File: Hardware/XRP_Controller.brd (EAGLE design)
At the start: 63.5 x 54 mm, 222 parts, among them J1 POWER_JACKPOWER_JACK_SLOT, J12 Vertical Qwiic Connector, J13 Vertical Qwiic Connector, J14 Vertical Qwiic Connector, J3 JST_6_PIN_VERTICAL, J4 JST_6_PIN_VERTICAL, J5 JST_6_PIN_VERTICAL, J6 JST_6_PIN_VERTICAL, J9 Vertical Qwiic Connector, Q3 20V/4.2A/52mΩ/1.4W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

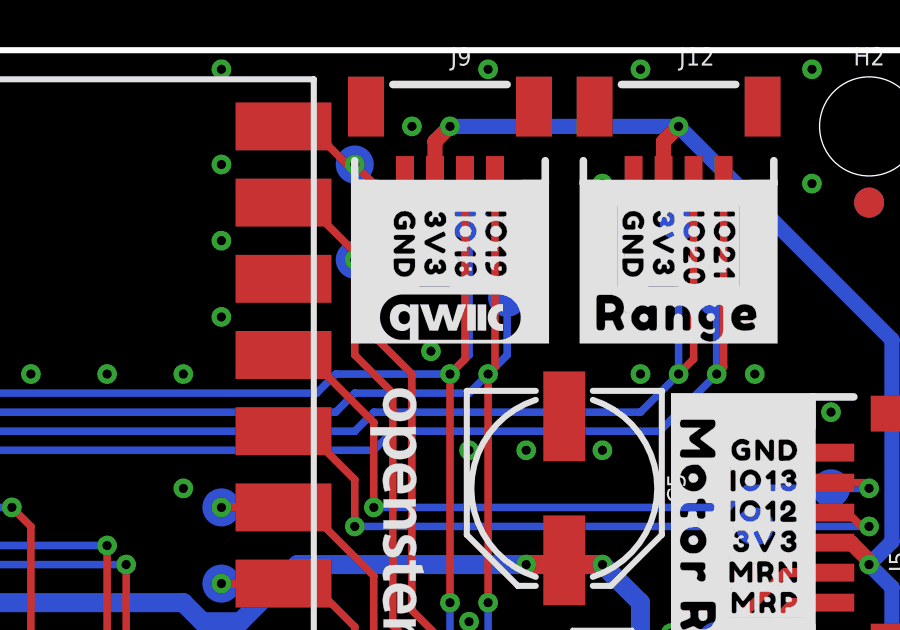
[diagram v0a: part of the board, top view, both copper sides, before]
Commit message: Add inverted Qwiic logo as library part
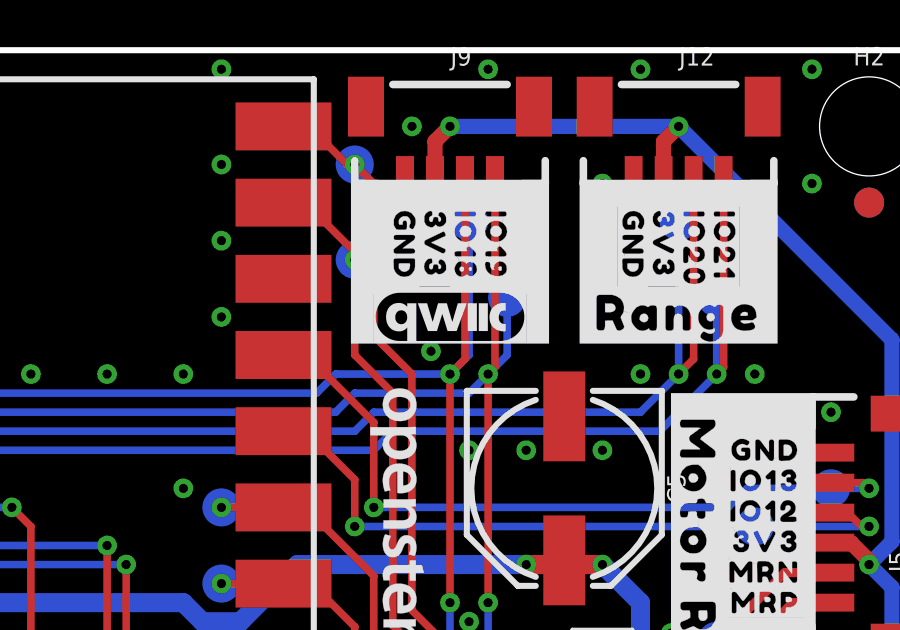
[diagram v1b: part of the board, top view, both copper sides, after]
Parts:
- added U$98: QWIIC_LOGO, XRP_COMPONENTS:QWIIC_INVERTED

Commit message: v09 tweaks
Ordering a few boards early before logos are finalized
Removed URLs for now
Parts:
- removed U$94: (no value), XRP_COMPONENTS:OPENSTEM_URL_SMALL
- removed U$97: (no value), XRP_COMPONENTS:OPENSTEM_URL_LARGE
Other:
- board text added: "v09"
- board text removed: "v10"
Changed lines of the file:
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@@
 <wire x1="63.5" y1="53.975" x2="0" y2="53.975" width="0.2032" layer="20"/>
 <wire x1="0" y1="53.975" x2="0" y2="0" width="0.2032" layer="20"/>
-<text x="31.75" y="1.27" size="1.778" layer="16" font="vector" ratio="15" rot="MR0" align="center">v10</text>
+<text x="31.75" y="1.27" size="1.778" layer="16" font="vector" ratio="15" rot="MR0" align="center">v09</text>
 <text x="35.56" y="-36.83" size="1.778" layer="51" font="vector">Dryw Wade</text>
 <rectangle x1="24.7396" y1="52.8066" x2="38.7604" y2="53.975" layer="41"/>
@@
 <rectangle x1="55.372" y1="44.196" x2="56.007" y2="44.2468" layer="21"/>
 <rectangle x1="52.197" y1="6.604" x2="52.324" y2="6.858" layer="41"/>
-<text x="31.75" y="1.27" size="1.778" layer="22" font="vector" ratio="15" rot="MR0" align="center">v10</text>
+<text x="31.75" y="1.27" size="1.778" layer="22" font="vector" ratio="15" rot="MR0" align="center">v09</text>
 </plain>
 <attributes>
@@
 <element name="U$73" library="output" package="#PWR#0" value="" x="62.23" y="9.525" smashed="yes" rot="MR90"/>
 <element name="U$72" library="XRP_COMPONENTS" package="OPENSTEM_LOGO" value="" x="27.305" y="24.511" smashed="yes" rot="MR0"/>
-<element name="U$94" library="XRP_COMPONENTS" package="OPENSTEM_URL_SMALL" value="" x="45.339" y="34.036" smashed="yes" rot="R270"/>
-<element name="U$97" library="XRP_COMPONENTS" package="OPENSTEM_URL_LARGE" value="" x="27.305" y="16.891" smashed="yes" rot="MR0"/>
 <element name="U$98" library="XRP_COMPONENTS" package="QWIIC_INVERTED" value="QWIIC_LOGO" x="46.99" y="45.085" smashed="yes"/>
 </elements>

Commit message: v10 updates
Bump version number to v10
Remove OpenSTEM logo
Add XRP URL to top and bottom silk
Nudge expansion connectors in schematic to not have overlapping labels
Nudge Qwiic logo to get thicker silk along bottom edge
Approve DRC overlap errors
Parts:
- added U$97: (no value), XRP_COMPONENTS:XRP_URL_5MM
- U$72: device XRP_COMPONENTS:OPENSTEM_LOGO -> XRP_COMPONENTS:XRP_URL_3MM
- moved U$72 21.1 mm to (45.5, 35.2), flipped to the top, turned to 270 degrees
- moved U$98 0.13 mm to (47.0, 45.2)
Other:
- board text added: "v10"
- board text removed: "v09"
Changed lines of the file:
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@@
 <wire x1="63.5" y1="53.975" x2="0" y2="53.975" width="0.2032" layer="20"/>
 <wire x1="0" y1="53.975" x2="0" y2="0" width="0.2032" layer="20"/>
-<text x="31.75" y="1.27" size="1.778" layer="16" font="vector" ratio="15" rot="MR0" align="center">v09</text>
+<text x="31.75" y="1.27" size="1.778" layer="16" font="vector" ratio="15" rot="MR0" align="center">v10</text>
 <text x="35.56" y="-36.83" size="1.778" layer="51" font="vector">Dryw Wade</text>
 <rectangle x1="24.7396" y1="52.8066" x2="38.7604" y2="53.975" layer="41"/>
@@
 <dimension x1="0" y1="0" x2="0" y2="53.975" x3="-27.94" y3="26.9875" textsize="1.778" textratio="15" layer="47" unit="inch" precision="3"/>
 <dimension x1="0" y1="53.975" x2="8.89" y2="53.975" x3="4.445" y3="55.86871875" textsize="1.778" textratio="15" layer="47" unit="inch"/>
-<dimension x1="0" y1="53.975" x2="16.51" y2="53.975" x3="8.255" y3="59.681090625" textsize="1.778" textratio="15" layer="47" unit="inch" precision="3"/>
-<dimension x1="0" y1="53.975" x2="46.99" y2="53.975" x3="23.495" y3="63.498203125" textsize="1.778" textratio="15" layer="47" unit="inch" precision="3"/>
+<dimension x1="0" y1="53.975" x2="16.51" y2="53.975" x3="8.255" y3="59.681090625" textsize="1.778" textratio="15" layer="47" unit="inch"/>
+<dimension x1="0" y1="53.975" x2="46.99" y2="53.975" x3="23.495" y3="63.498203125" textsize="1.778" textratio="15" layer="47" unit="inch"/>
 <dimension x1="0" y1="53.975" x2="54.61" y2="53.975" x3="27.305" y3="67.308153125" textsize="1.778" textratio="15" layer="47" unit="inch"/>
 <dimension x1="63.5" y1="0" x2="63.5" y2="22.86" x3="67.31" y3="11.43" textsize="1.778" textratio="15" layer="47" unit="inch"/>
@@
 <rectangle x1="54.356" y1="23.495" x2="55.88" y2="24.003" layer="21" rot="R180"/>
 <rectangle x1="54.356" y1="24.003" x2="54.483" y2="31.877" layer="21" rot="R180"/>
-<rectangle x1="49.022" y1="45.847" x2="50.292" y2="49.657" layer="21"/>
-<rectangle x1="43.688" y1="45.847" x2="44.958" y2="49.657" layer="21"/>
+<rectangle x1="49.022" y1="45.974" x2="50.292" y2="49.657" layer="21"/>
+<rectangle x1="43.688" y1="45.974" x2="44.958" y2="49.657" layer="21"/>
 <rectangle x1="44.958" y1="48.768" x2="49.022" y2="49.657" layer="21"/>
-<rectangle x1="44.958" y1="45.9232" x2="49.022" y2="46.101" layer="21"/>
-<rectangle x1="43.688" y1="44.2468" x2="44.45" y2="45.847" layer="21"/>
-<rectangle x1="49.53" y1="44.2468" x2="50.292" y2="45.847" layer="21"/>
-<rectangle x1="43.688" y1="44.196" x2="50.292" y2="44.2468" layer="21"/>
+<rectangle x1="44.958" y1="46.0502" x2="49.022" y2="46.101" layer="21"/>
+<rectangle x1="43.688" y1="44.3738" x2="44.45" y2="45.974" layer="21"/>
+<rectangle x1="49.53" y1="44.3738" x2="50.292" y2="45.974" layer="21"/>
+<rectangle x1="43.688" y1="44.196" x2="50.292" y2="44.3738" layer="21"/>
 <rectangle x1="18.542" y1="45.847" x2="19.812" y2="49.657" layer="21"/>
 <rectangle x1="13.208" y1="45.847" x2="14.478" y2="49.657" layer="21"/>
@@
 <rectangle x1="55.372" y1="44.196" x2="56.007" y2="44.2468" layer="21"/>
 <rectangle x1="52.197" y1="6.604" x2="52.324" y2="6.858" layer="41"/>
-<text x="31.75" y="1.27" size="1.778" layer="22" font="vector" ratio="15" rot="MR0" align="center">v09</text>
+<text x="31.75" y="1.27" size="1.778" layer="22" font="vector" ratio="15" rot="MR0" align="center">v10</text>
 </plain>
 <attributes>
@@
 <element name="U$96" library="output" package="#SYS#0" value="" x="59.436" y="10.795" smashed="yes" rot="MR0"/>
 <element name="U$73" library="output" package="#PWR#0" value="" x="62.23" y="9.525" smashed="yes" rot="MR90"/>
-<element name="U$72" library="XRP_COMPONENTS" package="OPENSTEM_LOGO" value="" x="27.305" y="24.511" smashed="yes" rot="MR0"/>
-<element name="U$98" library="XRP_COMPONENTS" package="QWIIC_INVERTED" value="QWIIC_LOGO" x="46.99" y="45.085" smashed="yes"/>
+<element name="U$98" library="XRP_COMPONENTS" package="QWIIC_INVERTED" value="QWIIC_LOGO" x="46.99" y="45.212" smashed="yes"/>
+<element name="U$72" library="XRP_COMPONENTS" package="XRP_URL_3MM" value="" x="45.466" y="35.179" smashed="yes" rot="R270"/>
+<element name="U$97" library="XRP_COMPONENTS" package="XRP_URL_5MM" value="" x="20.574" y="22.733" smashed="yes" rot="MR0"/>
 </elements>
 <signals>
@@
 <via x="26.035" y="29.845" extent="1-16" drill="0.3048"/>
 <via x="34.29" y="34.29" extent="1-16" drill="0.3048"/>
-<via x="31.115" y="22.225" extent="1-16" drill="0.3048"/>
+<via x="31.75" y="22.86" extent="1-16" drill="0.3048"/>
 <via x="29.21" y="17.78" extent="1-16" drill="0.3048"/>
 <via x="57.15" y="33.02" extent="1-16" drill="0.3048"/>
